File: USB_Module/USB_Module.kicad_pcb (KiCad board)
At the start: 2 copper layers, 27.3 x 25.2 mm, 5 parts, among them J1 USB_A, J3 Conn_01x02_Pin, J4 Conn_01x08_Socket, J5 Conn_01x10_Socket

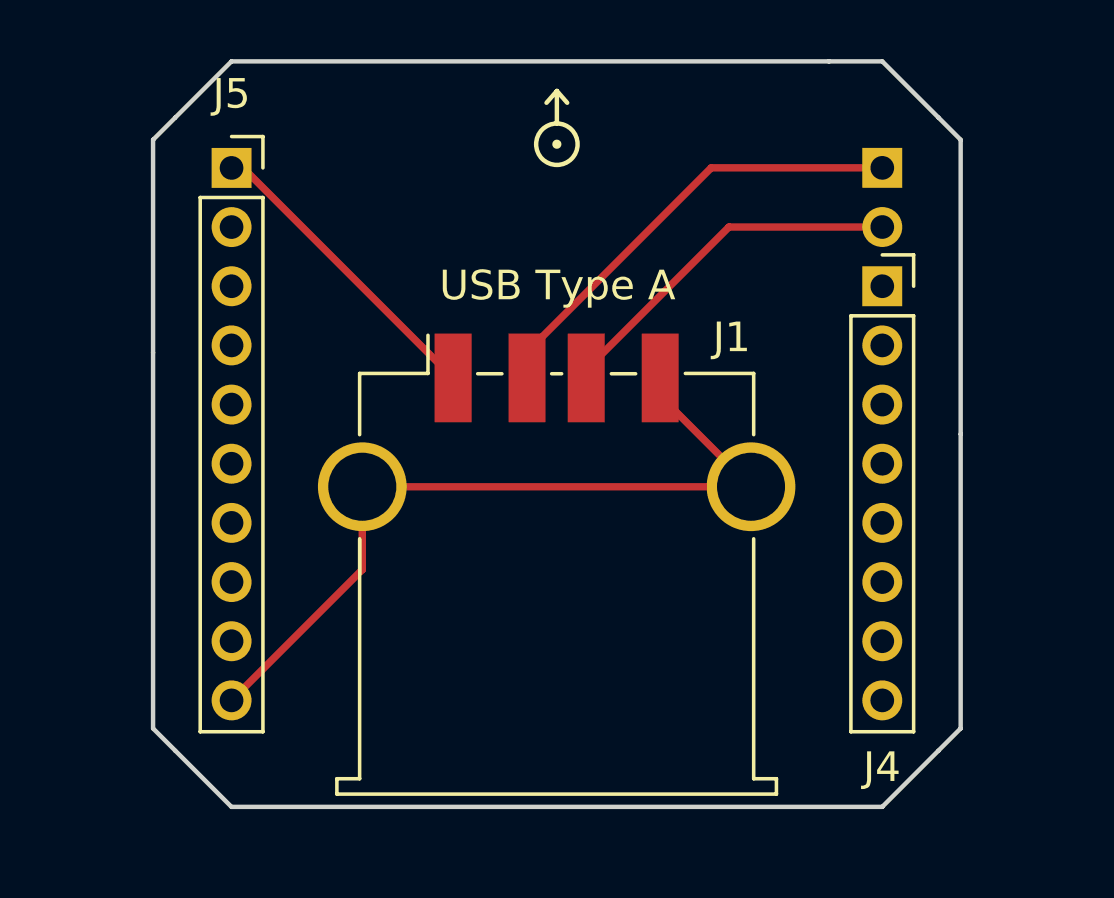
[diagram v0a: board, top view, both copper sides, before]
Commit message: Improving USB PCB design
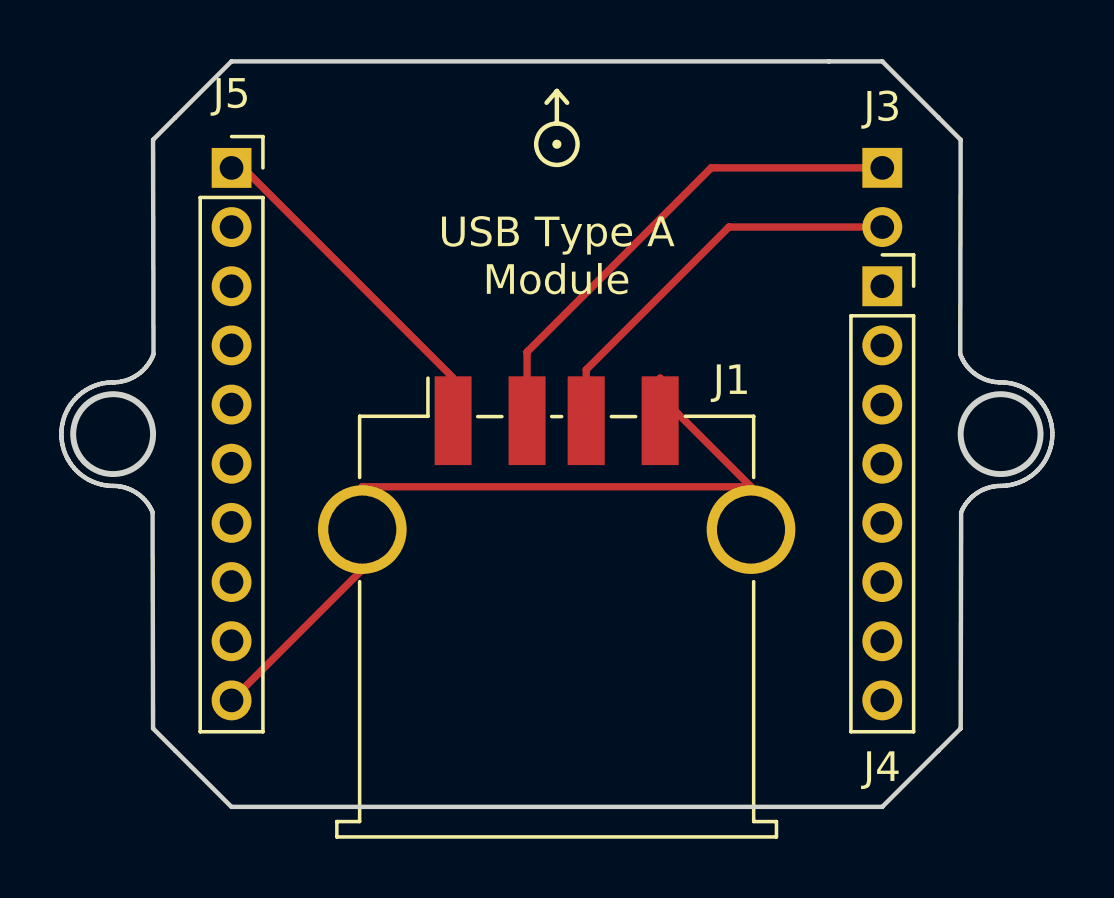
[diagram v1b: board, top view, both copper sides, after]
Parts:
- moved J1 1.45 mm to (144.3, 102.6)
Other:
- board size 27.3 x 25.2 mm -> 33.5 x 25.2 mm
- board text added: "USB Type A Module"
- board text removed: "USB Type A"

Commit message: Updating USB PCB desing
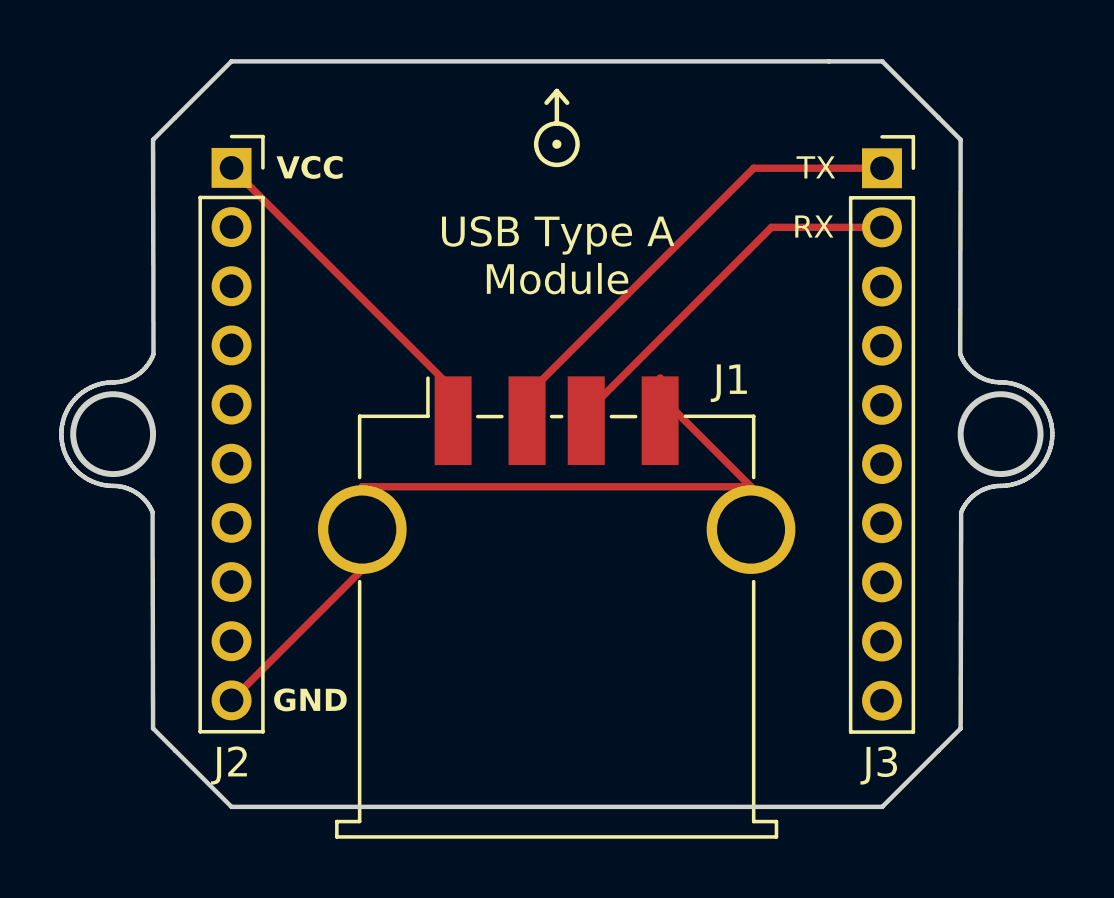
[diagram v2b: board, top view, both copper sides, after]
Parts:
- removed J4: Conn_01x08_Socket, Connector_PinSocket_2.00mm:PinSocket_1x08_P2.00mm_Vertical
- J3: value Conn_01x02_Pin -> Conn_01x10_Socket; footprint Connector_PinHeader_2.00mm:PinHeader_1x02_P2.00mm_Vertical -> Connector_PinSocket_2.00mm:PinSocket_1x10_P2.00mm_Vertical; moved to F.Cu
- turned J3 to 0 degrees
- renumbered J5 to J2
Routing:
- net Net-(J1-VBUS): track 10.4 -> 12.8 mm
- net Net-(J1-D-): track 15.5 -> 16.0 mm
- net Net-(J1-D+): track 12.3 -> 12.9 mm
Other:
- board text added: "GND"
- board text added: "RX"
- board text added: "TX"
- board text added: "VCC"

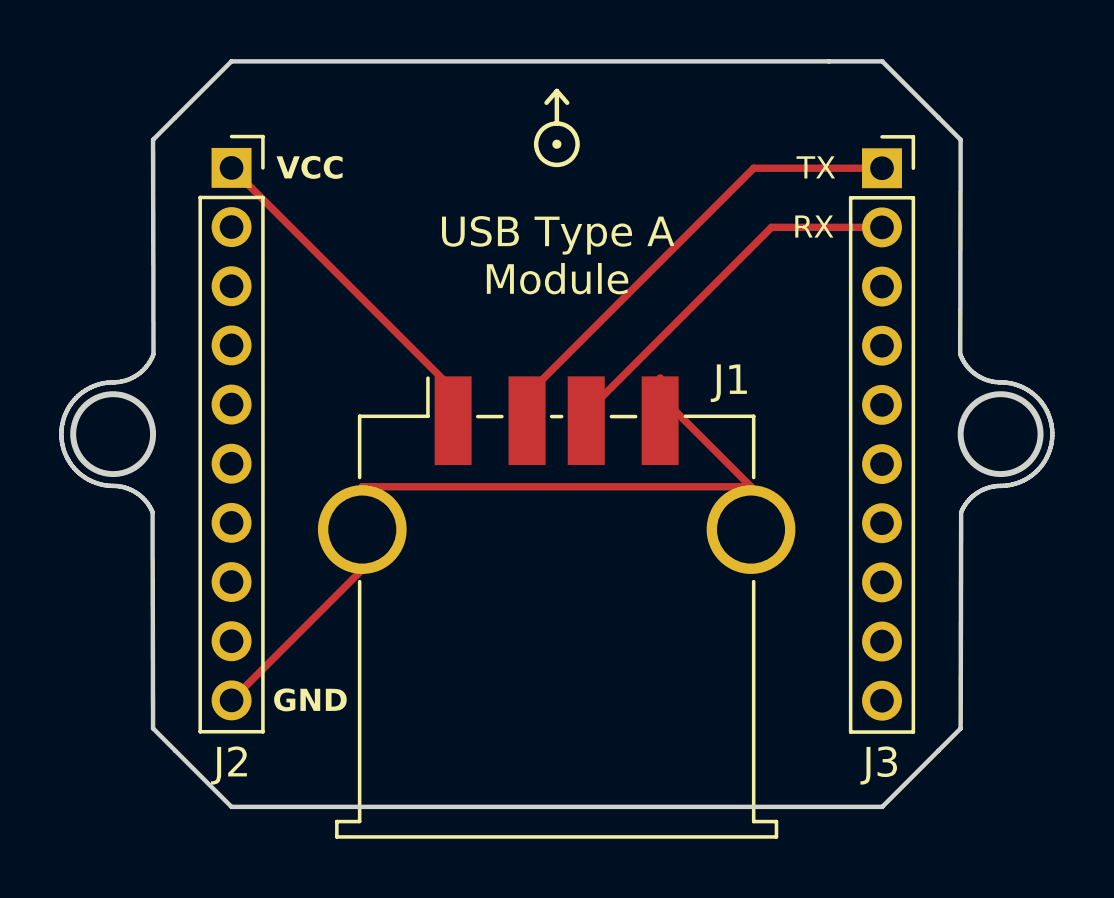
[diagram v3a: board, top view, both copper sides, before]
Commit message: Adding label pins in each PCB design
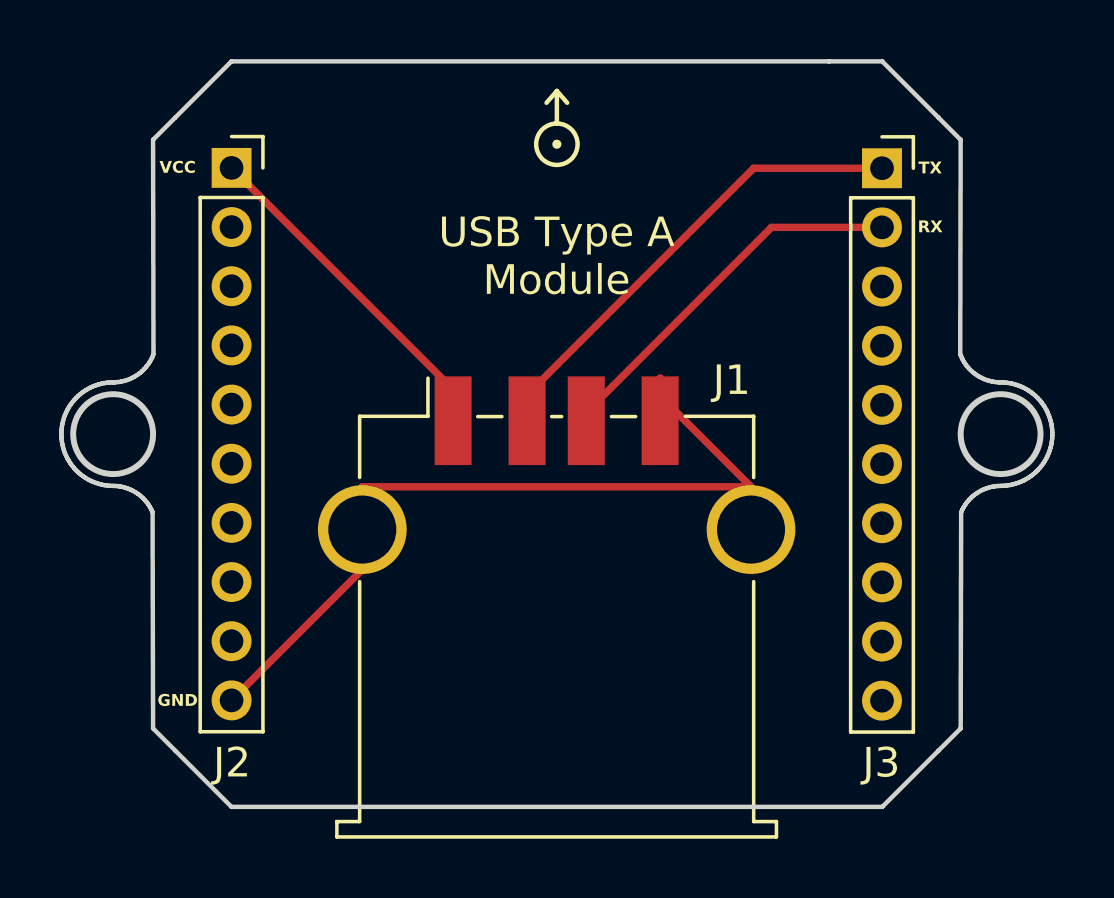
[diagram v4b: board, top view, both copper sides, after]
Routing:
- net Net-(J1-VBUS): track 12.8 -> 11.0 mm
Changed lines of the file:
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@@
         (effects (font (size 1 1) (thickness 0.15)))
     )
-    (fp_text value "USB_A" (at 0 9.09) (layer "F.Fab")
+    (fp_text value "USB_A" (at 0 9.09) (layer "F.Fab") hide
         (effects (font (size 1 1) (thickness 0.15)))
     )
@@
         (effects (font (size 1 1) (thickness 0.15)))
     )
-    (fp_text value "Conn_01x10_Socket" (at 0 20.5) (layer "F.Fab")
+    (fp_text value "Conn_01x10_Socket" (at 0 20.5) (layer "F.Fab") hide
         (effects (font (size 1 1) (thickness 0.15)))
     )
@@
         (effects (font (size 1 1) (thickness 0.15)))
     )
-    (fp_text value "Conn_01x10_Socket" (at 0 20.5) (layer "F.Fab")
+    (fp_text value "Conn_01x10_Socket" (at 0 20.5) (layer "F.Fab") hide
         (effects (font (size 1 1) (thickness 0.15)))
     )
@@
   (gr_line (start 160.960869 96.055073) (end 160.994422 96.149262)
     (stroke (width 0.15) (type solid)) (layer "Edge.Cuts"))
-  (gr_text "RX" (at 153 89.7) (layer "F.SilkS")
-    (effects (font (size 0.75 0.75) (thickness 0.15)))
+  (gr_text "GND" (at 131.51 105.69) (layer "F.SilkS")
+    (effects (font (size 0.4 0.4) (thickness 0.1) bold))
   )
   (gr_text "USB Type A\nModule" (at 144.3228 90.678) (layer "F.SilkS")
     (effects (font (size 1 1) (thickness 0.15)))
   )
-  (gr_text "GND" (at 136 105.7) (layer "F.SilkS")
-    (effects (font (size 0.75 0.75) (thickness 0.15) bold))
+  (gr_text "VCC" (at 131.51 87.67) (layer "F.SilkS")
+    (effects (font (size 0.4 0.4) (thickness 0.1) bold))
   )
-  (gr_text "TX" (at 153.1 87.7) (layer "F.SilkS")
-    (effects (font (size 0.75 0.75) (thickness 0.15)))
+  (gr_text "TX" (at 156.95 87.69) (layer "F.SilkS")
+    (effects (font (size 0.4 0.4) (thickness 0.1) bold))
   )
-  (gr_text "VCC" (at 136 87.7) (layer "F.SilkS")
-    (effects (font (size 0.75 0.75) (thickness 0.15) bold))
+  (gr_text "RX" (at 156.95 89.68) (layer "F.SilkS")
+    (effects (font (size 0.4 0.4) (thickness 0.1) bold))
   )
   (gr_text "M3" (at 157.8298 83.1892 -45) (layer "Eco1.User")
@@
     (effects (font (size 1 1) (thickness 0.25)))
   )
-  (segment (start 140.8228 95.1794) (end 140.8228 96.236) (width 0.25) (layer "F.Cu") (net 1))
   (segment (start 133.3336 87.6902) (end 133.7248 87.6902) (width 0.25) (layer "F.Cu") (net 1))
   (segment (start 133.3336 87.6902) (end 140.8228 95.1794) (width 0.25) (layer "F.Cu") (net 1))
-  (segment (start 141 95.3566) (end 141 96.1) (width 0.25) (layer "B.Cu") (net 1))
   (segment (start 155.321 87.7006) (end 150.9832 87.7006) (width 0.25) (layer "F.Cu") (net 2))
   (segment (start 143.3228 95.361) (end 143.3228 96.236) (width 0.25) (layer "F.Cu") (net 2))

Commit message: Adding FPV 4-pin interface module
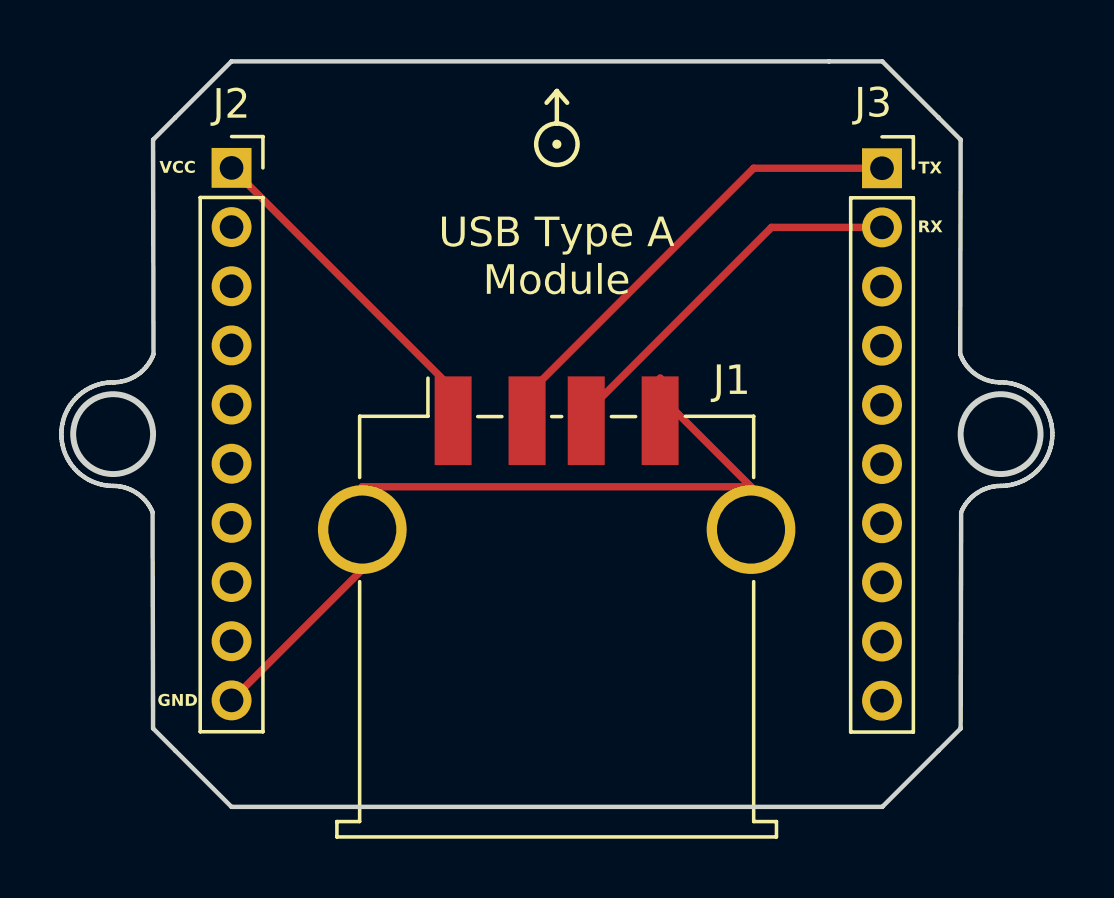
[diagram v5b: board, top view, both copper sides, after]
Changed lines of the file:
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@@
     (property "ki_keywords" "connector")
     (attr through_hole)
-    (fp_text reference "J2" (at 0.0164 20.1098) (layer "F.SilkS")
+    (fp_text reference "J2" (at -0.0036 -2.1602) (layer "F.SilkS")
         (effects (font (size 1 1) (thickness 0.15)))
     )
@@
     (property "ki_keywords" "connector")
     (attr through_hole)
-    (fp_text reference "J3" (at -0.021 20.0994) (layer "F.SilkS")
+    (fp_text reference "J3" (at -0.301 -2.2106) (layer "F.SilkS")
         (effects (font (size 1 1) (thickness 0.15)))
     )
